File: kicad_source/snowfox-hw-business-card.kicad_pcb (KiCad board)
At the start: 2 copper layers, 39 x 46 mm, 14 parts, among them CN1 TE_2041119-2, CN2 CONN_01X18, CN3 CONN_01X18

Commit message: started placement
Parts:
- removed G***: generationmake_logo, labels:generationmake_logo
- removed G***: generationmake_small_solder, labels:generationmake_small_solder
- removed MECH4, MECH5: MHP_3.2_5.8, MECH_mounting_holes:MHP_3.2_5.8
- removed W1, W2: TEST_1P, wire_pads:SolderWirePad_single_1mmSMD
- added BT1: Keystone 1043, MECH_battery_holder:KEYSTONE_1043, F.Cu at (81.0, 47.0)
- added BT2: Keystone 1043, MECH_battery_holder:KEYSTONE_1043, F.Cu at (187.0, 51.0)
- added C1: 100n, capacitors:C_0603, F.Cu at (253.3, 84.3)
- added C10: 100n, capacitors:C_0603, F.Cu at (253.3, 86.9)
- added C11: 100n, capacitors:C_0603, F.Cu at (250.0, 90.0)
- added C12: 100n, capacitors:C_0603, F.Cu at (257.2, 82.9)
- added C13: 100n, capacitors:C_0603, F.Cu at (245.8, 97.6)
- added C14: 100n, capacitors:C_0603, F.Cu at (264.5, 80.3)
- added C15: 100n, capacitors:C_0603, F.Cu at (257.2, 85.4)
- added C16: 100n, capacitors:C_0603, F.Cu at (249.7, 92.5)
- added C17: 100n, capacitors:C_0603, F.Cu at (264.5, 77.8)
- added C18: 1u 50V, capacitors:C_0603, F.Cu at (240.8, 109.5)
- added C19: 1u 50V, capacitors:C_0603, F.Cu at (240.6, 104.4)
- added C2: 100n, capacitors:C_0603, F.Cu at (256.6, 77.8)
- added C20: 1u 50V, capacitors:C_0603, F.Cu at (236.5, 113.7)
- added C21: 1u 50V, capacitors:C_0603, F.Cu at (244.8, 107.0)
- added C22: 1u 50V, capacitors:C_0603, F.Cu at (240.8, 107.0)
- added C23: 1u 50V, capacitors:C_0603, F.Cu at (244.5, 104.4)
- added C24: 1u 50V, capacitors:C_0603, F.Cu at (236.9, 110.1)
- added C25: 1u 50V, capacitors:C_0603, F.Cu at (227.0, 115.8)
- added C26: 1u 50V, capacitors:C_0603, F.Cu at (232.5, 113.7)
- added C27: 470n 50V, capacitors:C_0603, F.Cu at (236.9, 107.6)
- added C28: 10u, capacitors:C_0603, F.Cu at (183.8, 127.1)
- added C29: 100n, capacitors:C_0603, F.Cu at (183.4, 131.3)
- added C3: 15p, capacitors:C_0603, F.Cu at (256.6, 80.3)
- added C30: 10u, capacitors:C_0603, F.Cu at (197.6, 119.7)
- added C31: 100n, capacitors:C_0603, F.Cu at (179.5, 131.3)
- added C32: 1u, capacitors:C_0603, F.Cu at (189.7, 113.2)
- added C33: 1u, capacitors:C_0603, F.Cu at (219.6, 112.6)
- added C34: 1u, capacitors:C_0603, F.Cu at (215.7, 112.6)
- added C35: 1u, capacitors:C_0603, F.Cu at (219.6, 110.1)
- added C36: 1u, capacitors:C_0603, F.Cu at (215.7, 110.1)
- added C37: 100u/6.3V, capacitors:TantalC_SizeD_EIA-7343_Reflow, F.Cu at (182.6, 111.9)
- added C38: 100u/6.3V, capacitors:TantalC_SizeD_EIA-7343_Reflow, F.Cu at (214.8, 79.6)
- added C39: DNI, capacitors:C_0603, F.Cu at (121.0, 120.0)
- added C4: 15p, capacitors:C_0603, F.Cu at (246.1, 90.0)
- added C40: 100nF, capacitors:C_0603, F.Cu at (117.0, 115.0)
- added C5: 10u, capacitors:C_0603, F.Cu at (260.6, 77.8)
- added C6: 10u, capacitors:C_0603, F.Cu at (245.8, 92.5)
- added C7: 100n, capacitors:C_0603, F.Cu at (260.6, 80.3)
- added C8: 100n, capacitors:C_0603, F.Cu at (249.7, 95.1)
- added C9: 100n, capacitors:C_0603, F.Cu at (245.8, 95.1)
- added D2: MBR0530, diodes:SOD-123, F.Cu at (235.8, 104.7)
- added D3: MBR0530, diodes:SOD-123, F.Cu at (227.8, 109.8)
- added D4: MBR0530, diodes:SOD-123, F.Cu at (227.8, 112.9)
- added D5: green, LEDs:LED_0603, F.Cu at (187.3, 131.3)
- added D6: red, LEDs:LED_0603, F.Cu at (201.5, 119.7)
- added D7: MBR0530, diodes:SOD-123, F.Cu at (190.5, 110.4)
- added D8: 1N4148, diodes:SOD-123, F.Cu at (201.6, 110.4)
- added D9: 1N4148, diodes:SOD-123, F.Cu at (196.1, 110.4)
- added L1: INDUCTOR_SMALL, inductors:Inductor_1212, F.Cu at (229.0, 105.7)
- added P1: USB_OTG, CON_wuerth:WE_629105136821, F.Cu at (158.0, 104.0)
- added Q1: SI1304BDL, SOT_TO:SOT-23, F.Cu at (232.7, 110.3)
- added Q2: BC847, SOT_TO:SOT-23, F.Cu at (179.7, 127.9)
- added Q3: BC847, SOT_TO:SOT-23, F.Cu at (190.5, 127.9)
- added R10: 10k, resistors:R_0603, F.Cu at (257.5, 88.0)
- added R11: 10k, resistors:R_0603, F.Cu at (249.6, 97.7)
- added R12: 10k, resistors:R_0603, F.Cu at (253.8, 92.1)
- added R13: 10k, resistors:R_0603, F.Cu at (253.8, 89.5)
- added R14: 10k, resistors:R_0603, F.Cu at (261.0, 82.9)
- added R15: 2R2, resistors:R_0603, F.Cu at (240.3, 115.4)
- added R16: DNI, resistors:R_0603, F.Cu at (244.6, 109.6)
- added R17: 0R, resistors:R_0603, F.Cu at (240.3, 112.7)
- added R18: 22k1, resistors:R_0603, F.Cu at (201.8, 124.9)
- added R19: 47k5, resistors:R_0603, F.Cu at (198.4, 127.6)
- added R2: 100k, resistors:R_0603, F.Cu at (264.8, 85.6)
- added R20: 1k, resistors:R_0603, F.Cu at (198.4, 130.2)
- added R21: 1k, resistors:R_0603, F.Cu at (194.5, 127.1)
- added R22: 100R, resistors:R_0603, F.Cu at (194.7, 129.7)
- added R23: 100R, resistors:R_0603, F.Cu at (198.1, 124.9)
- added R24: 1k, resistors:R_0603, F.Cu at (201.1, 122.3)
- added R25: 10k, resistors:R_0603, F.Cu at (191.1, 131.3)
- added R26: 10k, resistors:R_0603, F.Cu at (197.5, 122.3)
- added R27: 150k, resistors:R_0603, F.Cu at (193.5, 113.3)
- added R28: 10k, resistors:R_0603, F.Cu at (120.0, 110.0)
- added R3: 1M, resistors:R_0603, F.Cu at (253.2, 97.7)
- added R4: 100R, resistors:R_0603, F.Cu at (261.1, 88.2)
- added R5: 100R, resistors:R_0603, F.Cu at (257.5, 93.3)
- added R6: 100R, resistors:R_0603, F.Cu at (261.1, 85.6)
- added R7: 100R, resistors:R_0603, F.Cu at (264.7, 82.9)
- added R8: 100, resistors:R_0603, F.Cu at (253.5, 94.8)
- added R9: 10k, resistors:R_0603, F.Cu at (257.5, 90.7)
- added SW1: TAST_VER, mechanical-switches:WE_430182050816, F.Cu at (144.0, 133.0)
- added SW2: TAST_VER, mechanical-switches:WE_430182050816, F.Cu at (84.0, 133.0)
- added SW3: TAST_VER, mechanical-switches:WE_430182050816, F.Cu at (101.0, 133.0)
- added SW4: TAST_VER, mechanical-switches:WE_430182050816, F.Cu at (156.0, 133.0)
- added SW5: SWITCH_INV, mechanical-switches:WE_450404015514, F.Cu at (150.0, 85.0)
- added U1: W25Q80D, SOIC:SOIC-8_3.9x4.9mm_Pitch1.27mm, F.Cu at (96.0, 98.0)
- added U2: ATECC608A, SOIC:SOIC-8_3.9x4.9mm_Pitch1.27mm, F.Cu at (239.8, 87.1)
- added U3: FE310-G002, QFN:QFN-48-1EP_6x6mm_P0.4mm_EP4.3x4.3mm, F.Cu at (105.0, 103.0)
- added U4: CP2102N_28, QFN:QFN-28-1EP_5x5mm_Pitch0.5mm, F.Cu at (148.8, 104.2)
- added U5: TPS736XX, SOT_TO:SOT-23-5, F.Cu at (211.4, 111.2)
- added U6: TPS736XX, SOT_TO:SOT-23-5, F.Cu at (206.7, 111.2)
- added U7: M24LR, SOIC:SOIC-8_3.9x4.9mm_Pitch1.27mm, F.Cu at (121.0, 115.0)
- added Y1: Crystal_SMD_4Pad, crystals:Crystal_SMD_0603_4Pads, F.Cu at (247.7, 86.3)
- CN1: value TE_2041119-2 -> Micro_SDCard; footprint connectors_pci-express:MPCIe_4mm -> CON_wuerth:WE_693071010811
- CN2: value CONN_01X18 -> CONN_02X05; footprint pin_headers:Pin_Header_Straight_1x18 -> pin_headers:Pin_Header_Straight_2x05_Pitch1.27mm
- CN3: value CONN_01X18 -> CONN_01X24; footprint pin_headers:Pin_Header_Straight_1x18 -> pin_headers:Pin_Header_Angled_1x24_Pitch1.00mm
- D1: value 150060YS75000 -> blue
- MECH1, MECH2: value WA-SMSI_9774015151 -> MHP_3.2_5.8; footprint MECH_smd-spacer:WA-SMSI_9774015151 -> MECH_mounting_holes:MHP_3.2_5.8
- R1: value 3k3 -> 1k
- moved MECH3 151.8 mm to (238.3, 64.9)
- moved MECH2 132.1 mm to (231.5, 64.9)
- moved R1 118.7 mm to (194.4, 92.2), turned to 0 degrees
- moved D1 110.8 mm to (189.0, 100.6), turned to 0 degrees
- moved MECH1 77.4 mm to (159.0, 87.0)
- moved CN3 60.5 mm to (80.0, 97.0), turned to 0 degrees
- moved CN2 42.8 mm to (102.0, 113.0), turned to 90 degrees
- moved CN1 42.4 mm to (124.0, 99.0), turned to 180 degrees
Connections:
- CN1 pad 1: /PEX_PIN1 -> (no net)
- CN1 pad 10: /PEX_PIN10 -> (no net)
- CN1 pad 2: +3V3 -> /Microcontroller/SPI_CS_SD_R
- CN1 pad 3: /PEX_PIN3 -> /Microcontroller/SPI_MOSI_R
- CN1 pad 4: GND -> +3V3
- CN1 pad 5: /PEX_PIN5 -> /Microcontroller/SPI_CLK_R
- CN1 pad 6: /PEX_PIN6 -> GND
- CN1 pad 7: /PEX_PIN7 -> /Microcontroller/SPI_MISO_R
- CN1 pad 8: /PEX_PIN8 -> (no net)
- CN1 pad 9: GND -> (no net)
- CN2 pad 1: +3V3 -> (no net)
- CN2 pad 10: /PEX_PIN12 -> RESET
- CN2 pad 2: /PEX_PIN1 -> /Microcontroller/JTAG_TMS
- CN2 pad 3: /PEX_PIN3 -> GND
- CN2 pad 4: /PEX_PIN5 -> /Microcontroller/JTAG_TCK
- CN2 pad 5: /PEX_PIN6 -> GND
- CN2 pad 6: /PEX_PIN7 -> /Microcontroller/JTAG_TDO
- CN2 pad 7: /PEX_PIN8 -> (no net)
- CN2 pad 8: /PEX_PIN10 -> /Microcontroller/JTAG_TDI
- CN2 pad 9: /PEX_PIN11 -> (no net)
- CN3 pad 1: +3V3 -> (no net)
- CN3 pad 10: /PEX_PIN33 -> DIS_RESET#
- CN3 pad 11: /PEX_PIN32 -> DIS_D_C#
- CN3 pad 12: /PEX_PIN31 -> SPI_CS_DIS
- CN3 pad 13: /PEX_PIN30 -> SPI_CLK
- CN3 pad 14: /PEX_PIN28 -> SPI_MOSI
- CN3 pad 15: /PEX_PIN25 -> +3V3
- CN3 pad 16: /PEX_PIN23 -> +3V3
- CN3 pad 18: GND -> /Display/VDD
- CN3 pad 2: /PEX_PIN51 -> /Display/GDR
- CN3 pad 3: /PEX_PIN49 -> /Display/RESE
- CN3 pad 4: /PEX_PIN48 -> (no net)
- CN3 pad 5: /PEX_PIN47 -> /Display/VSH2
- CN3 pad 6: /PEX_PIN46 -> (no net)
- CN3 pad 7: /PEX_PIN45 -> (no net)
- CN3 pad 8: /PEX_PIN44 -> /Display/BSI
- CN3 pad 9: /PEX_PIN42 -> DIS_BUSY
- R1 pad 2: +3V3 -> /Microcontroller/LED
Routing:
- net +3V3: track 101.7 -> 0.00 mm, vias 6 -> 0
- net /NFC/ANTENNA: track 0.00 -> 93.2 mm
- net GND: track 66.1 -> 0.00 mm, vias 15 -> 0
- net /PEX_PIN23: track 35.2 -> 0.00 mm, vias 1 -> 0
- net /PEX_RST: track 32.0 -> 0.00 mm
- net /PEX_PIN25: track 31.8 -> 0.00 mm, vias 1 -> 0
- net /WM_PIO25: track 30.5 -> 0.00 mm
- net /WM_PIO24: track 29.0 -> 0.00 mm
- net /PEX_PIN20: track 26.3 -> 0.00 mm
- net /PEX_PIN48: track 23.5 -> 0.00 mm, vias 1 -> 0
- net /PEX_PIN28: track 23.1 -> 0.00 mm
- net /PEX_PIN31: track 22.8 -> 0.00 mm, vias 1 -> 0
- net /PEX_PIN46: track 19.9 -> 0.00 mm, vias 1 -> 0
- net /PEX_PIN30: track 19.8 -> 0.00 mm
- net /PEX_PIN13: track 18.1 -> 0.00 mm
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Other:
- board size 39 x 46 mm -> 85 x 54 mm
- board text removed: "3V3"
- board text removed: "GND"
- board text removed: "Licensed under CERN OHL v.1.2"
- board text removed: "P1"
- board text removed: "P10"
- board text removed: "P10 (3)"
- board text removed: "P11"
- board text removed: "P11(19)"
- board text removed: "P12"
- board text removed: "P12(4)"
- board text removed: "P13"
- board text removed: "P13(20)"
- board text removed: "P14"
- board text removed: "P14(5)"
- board text removed: "P16"
- board text removed: "P16(6)"
- board text removed: "P20"
- board text removed: "P20(7)"
- board text removed: "P23"
- board text removed: "P23(21)"
- board text removed: "P25"
- board text removed: "P25(22)"
- board text removed: "P28"
- board text removed: "P28(8)"
- board text removed: "P3"
- board text removed: "P30"
- board text removed: "P30(9)pu"
- board text removed: "P31"
- board text removed: "P31(23)"
- board text removed: "P32"
- board text removed: "P32(10)pu"
- board text removed: "P33"
- board text removed: "P33(24)"
- board text removed: "P42"
- board text removed: "P42(11)"
- board text removed: "P44"
- board text removed: "P44(12)"
- board text removed: "P45"
- board text removed: "P45(13)"
- board text removed: "P46"
- board text removed: "P46(14)"
- board text removed: "P47"
- board text removed: "P47(15)"
- board text removed: "P48"
- board text removed: "P48(16)"
- board text removed: "P49"
- board text removed: "P49 (17)"
- board text removed: "P5"
- board text removed: "P51"
- board text removed: "P51 (18)"
- board text removed: "P6"
- board text removed: "P6(1)"
- board text removed: "P7"
- board text removed: "P8"
- board text removed: "P8(2)"
- board text removed: "PWR"
- board text removed: "RST"
- board text removed: "RST (0)pu"
- board text removed: "VidorBreakout 1.0"
- board text removed: "WM_PIO24"
- board text removed: "WM_PIO25"
- board text removed: "bot"
- board text removed: "top"
- board text removed: "use with Arduino MKR Vidor 4000"
- board text removed: "visit www.generationmake.de for more information!"

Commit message: made first placement
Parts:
- BT1, BT2: value Keystone 1043 -> 79523141; footprint MECH_battery_holder:KEYSTONE_1043 -> MECH_battery_holder:Wuerth_WA-BCMC_79523141
- moved R2 177.9 mm to (88.0, 106.0), turned to 90 degrees
- moved C15 171.9 mm to (92.0, 133.0)
- moved R7 171.5 mm to (97.0, 119.0)
- moved R4 168.2 mm to (97.0, 125.0)
- moved C3 168.0 mm to (92.0, 114.0), turned to 180 degrees
- moved R6 167.9 mm to (97.0, 121.0)
- moved R12 166.4 mm to (92.0, 131.0)
- moved C1 164.7 mm to (90.0, 106.0), turned to 270 degrees
- moved C5 164.2 mm to (99.0, 107.0), turned to 180 degrees
- moved C16 163.3 mm to (92.0, 135.0)
- moved R5 163.2 mm to (97.0, 123.0)
- moved R16 162.3 mm to (83.0, 95.0), turned to 270 degrees
- moved C21 160.8 mm to (84.0, 110.0), turned to 180 degrees
- moved C23 160.6 mm to (84.0, 108.0)
- moved MECH3 158.3 mm to (81.5, 86.5)
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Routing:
- net /NFC/ANTENNA: track 93.2 -> 250.4 mm, vias 0 -> 2

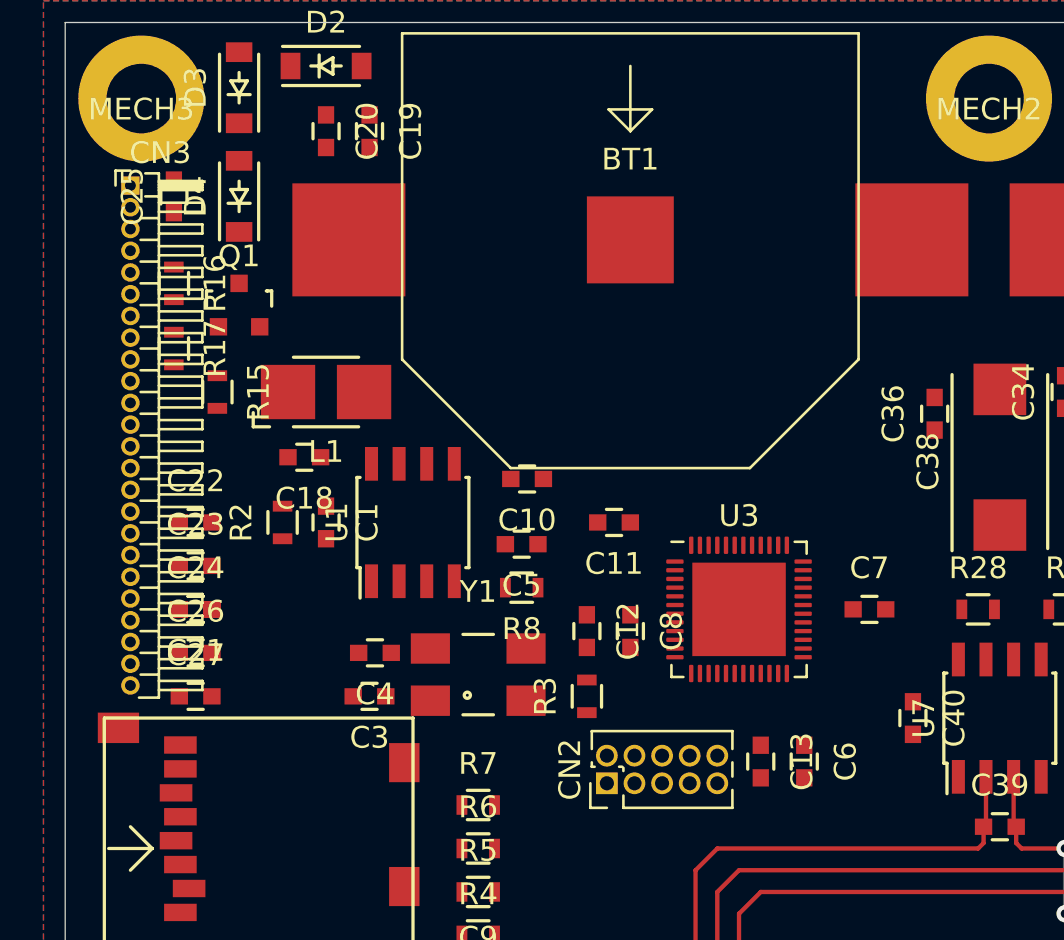
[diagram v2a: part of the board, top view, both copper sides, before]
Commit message: changed connector for display
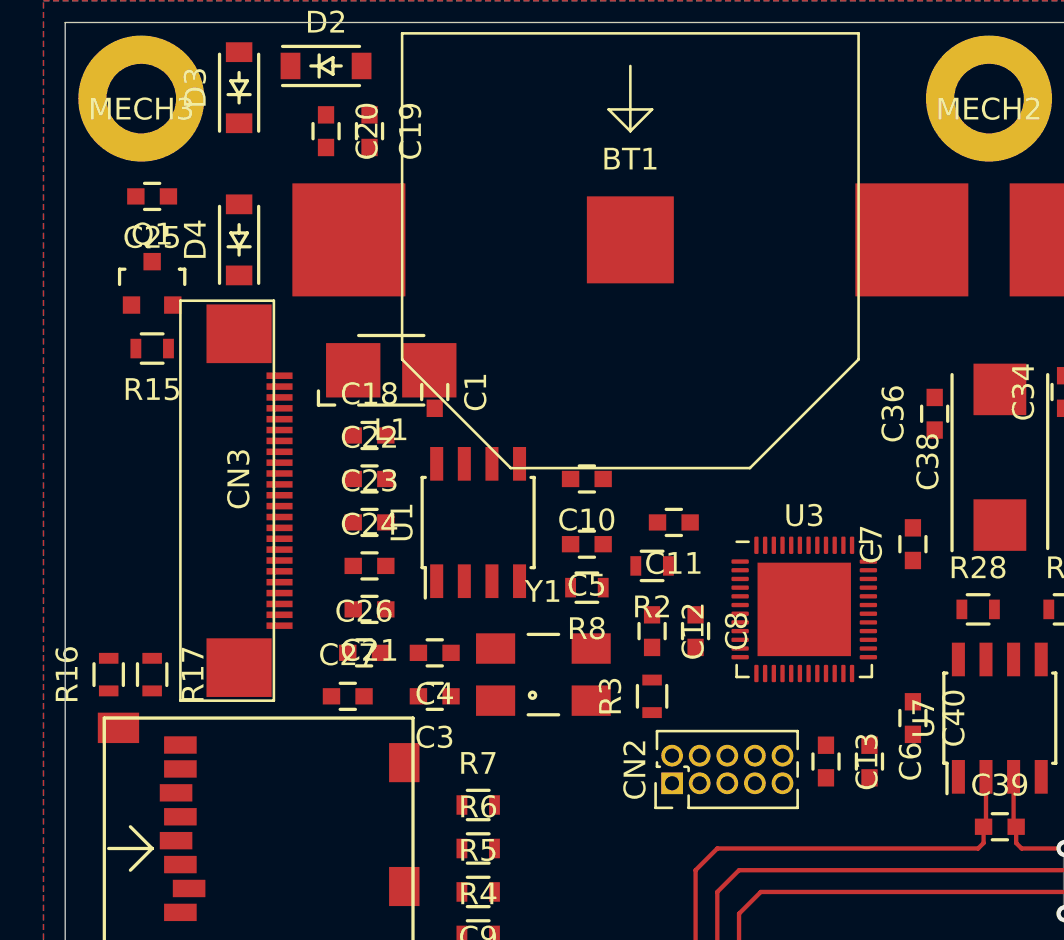
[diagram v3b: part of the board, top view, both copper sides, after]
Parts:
- CN3: footprint pin_headers:Pin_Header_Angled_1x24_Pitch1.00mm -> CON_wuerth:WR-FPC_68712414522
- Y1: value Crystal_SMD_4Pad -> 16MHz
- moved R16 18.2 mm to (80.0, 113.0), turned to 90 degrees
- moved R2 17.1 mm to (105.0, 108.0), turned to 180 degrees
- moved CN3 15.3 mm to (86.0, 105.0), turned to 270 degrees
- moved R17 15.0 mm to (82.0, 113.0)
- moved C22 8.25 mm to (92.0, 104.0)
- moved C23 8.25 mm to (92.0, 106.0)
- moved C24 8.25 mm to (92.0, 108.0)
- moved C21 8.00 mm to (92.0, 110.0)
- moved C1 7.81 mm to (95.0, 100.0)
- moved C26 7.75 mm to (91.8, 112.0)
- moved C27 7.00 mm to (91.0, 114.0)
- moved Q1 4.12 mm to (82.0, 95.0)
- moved C7 3.61 mm to (117.0, 107.0), turned to 90 degrees
- moved R15 3.61 mm to (82.0, 98.0), turned to 180 degrees
- moved C18 3.16 mm to (92.0, 102.0), turned to 0 degrees
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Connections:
- CN2 pad 1: (no net) -> +3V3

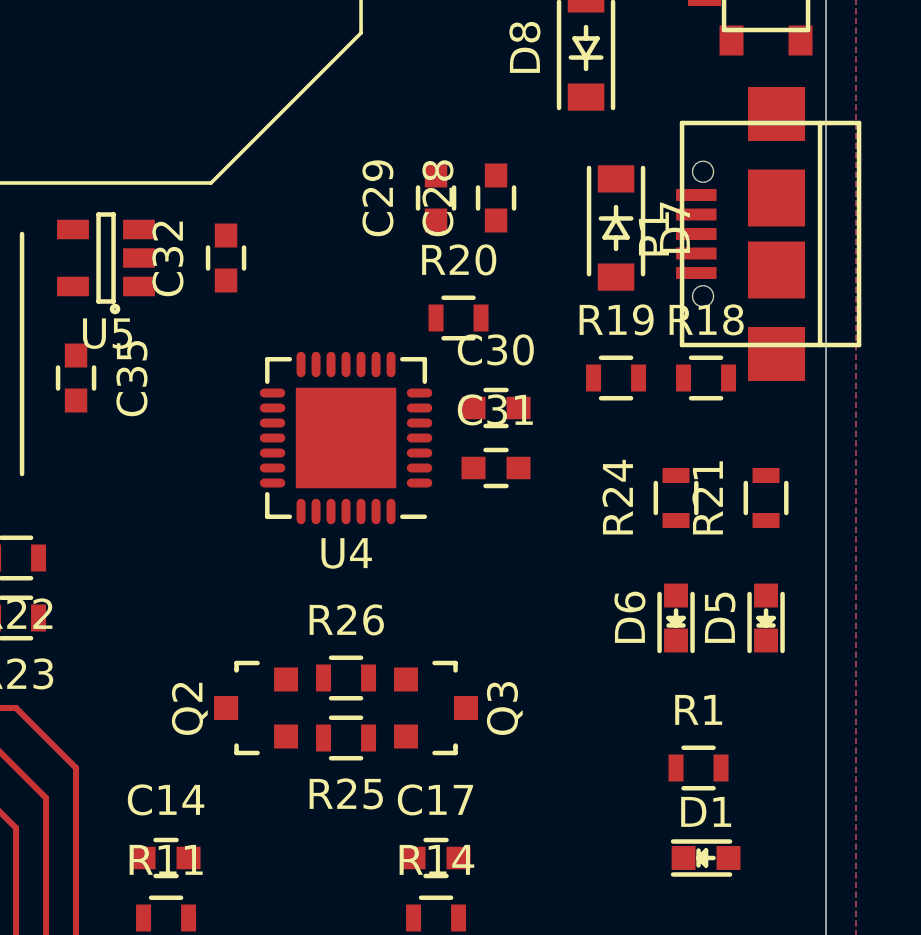
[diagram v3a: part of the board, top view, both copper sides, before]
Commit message: changed usb controller to FTDI FT230XS
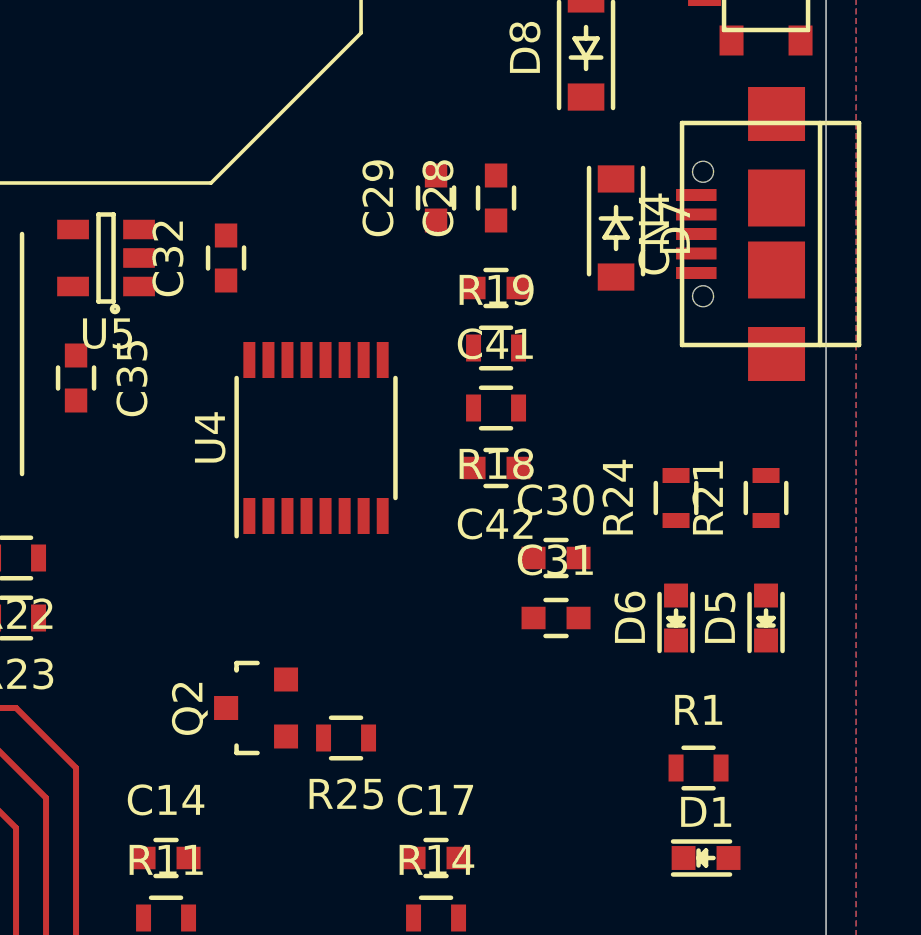
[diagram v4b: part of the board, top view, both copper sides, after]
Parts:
- removed Q3: BC847, SOT_TO:SOT-23
- removed R20: 1k, resistors:R_0603
- removed R26: 10k, resistors:R_0603
- added C41: 47pF, capacitors:C_0603, F.Cu at (152.0, 107.0)
- added C42: 47pF, capacitors:C_0603, F.Cu at (152.0, 113.0)
- R18: value 22k1 -> 27R
- R19: value 47k5 -> 27R
- U4: value CP2102N_28 -> FT230XS; footprint QFN:QFN-28-1EP_5x5mm_Pitch0.5mm -> SSOP:SSOP-16_3.9x4.9mm_Pitch0.635mm
- moved R18 7.07 mm to (152.0, 111.0), turned to 180 degrees
- moved C30 5.39 mm to (154.0, 116.0)
- moved C31 5.39 mm to (154.0, 118.0)
- moved R19 4.12 mm to (152.0, 109.0)
- moved U4 1.00 mm to (146.0, 112.0), turned to 90 degrees
- renumbered P1 to CN4
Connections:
- CN4 pad 2: Net-(P1-Pad2) -> /USB/USBDM
- CN4 pad 3: Net-(P1-Pad3) -> /USB/USBDP
- D5 pad 1: Net-(D5-Pad1) -> /USB/RX_LED
- D6 pad 1: Net-(D6-Pad1) -> /USB/TX_LED
- Q2 pad 1: /USB/DTR_R -> /USB/RTS_R
- Q2 pad 2: /USB/RTS -> GND
- R18 pad 1: Net-(R18-Pad1) -> /USB/USBDM
- R18 pad 2: VIN -> /USB/USBDM_R
- R19 pad 1: GND -> /USB/USBDP_R
- R19 pad 2: Net-(R18-Pad1) -> /USB/USBDP
- R25 pad 1: /USB/DTR -> /USB/RTS
- R25 pad 2: /USB/DTR_R -> /USB/RTS_R
- U4 pad 1: (no net) -> /USB/TX_R
- U4 pad 10: (no net) -> VIO
- U4 pad 11: (no net) -> VIO
- U4 pad 12: (no net) -> VIN
- U4 pad 13: (no net) -> GND
- U4 pad 14: (no net) -> /USB/RX_LED
- U4 pad 2: (no net) -> /USB/RTS
- U4 pad 3: GND -> VIO
- U4 pad 4: Net-(P1-Pad3) -> /USB/RX_R
- U4 pad 5: Net-(P1-Pad2) -> GND
- U4 pad 6: VIO -> (no net)
- U4 pad 7: VIN -> /USB/TX_LED
- U4 pad 8: Net-(R18-Pad1) -> /USB/USBDP_R
- U4 pad 9: Net-(R20-Pad1) -> /USB/USBDM_R

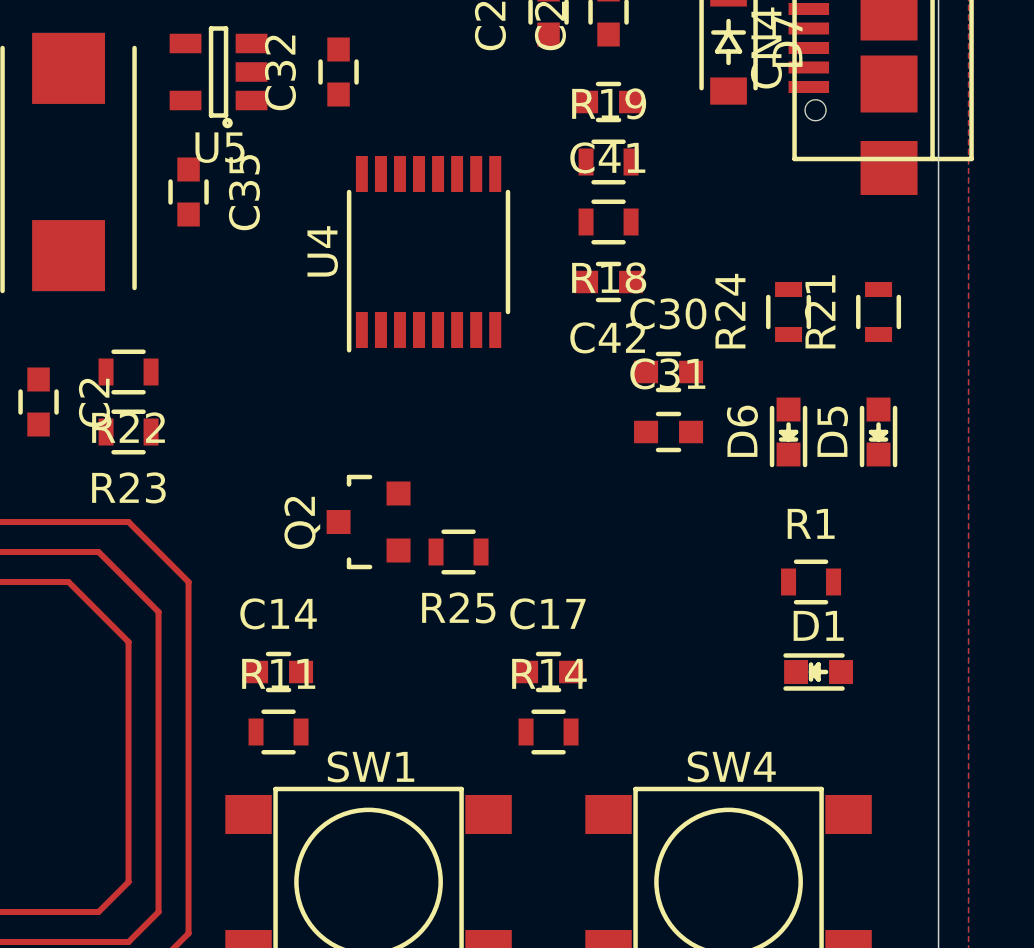
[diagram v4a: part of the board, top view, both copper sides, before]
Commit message: added qwiic connector for I2C and grove connector for UART
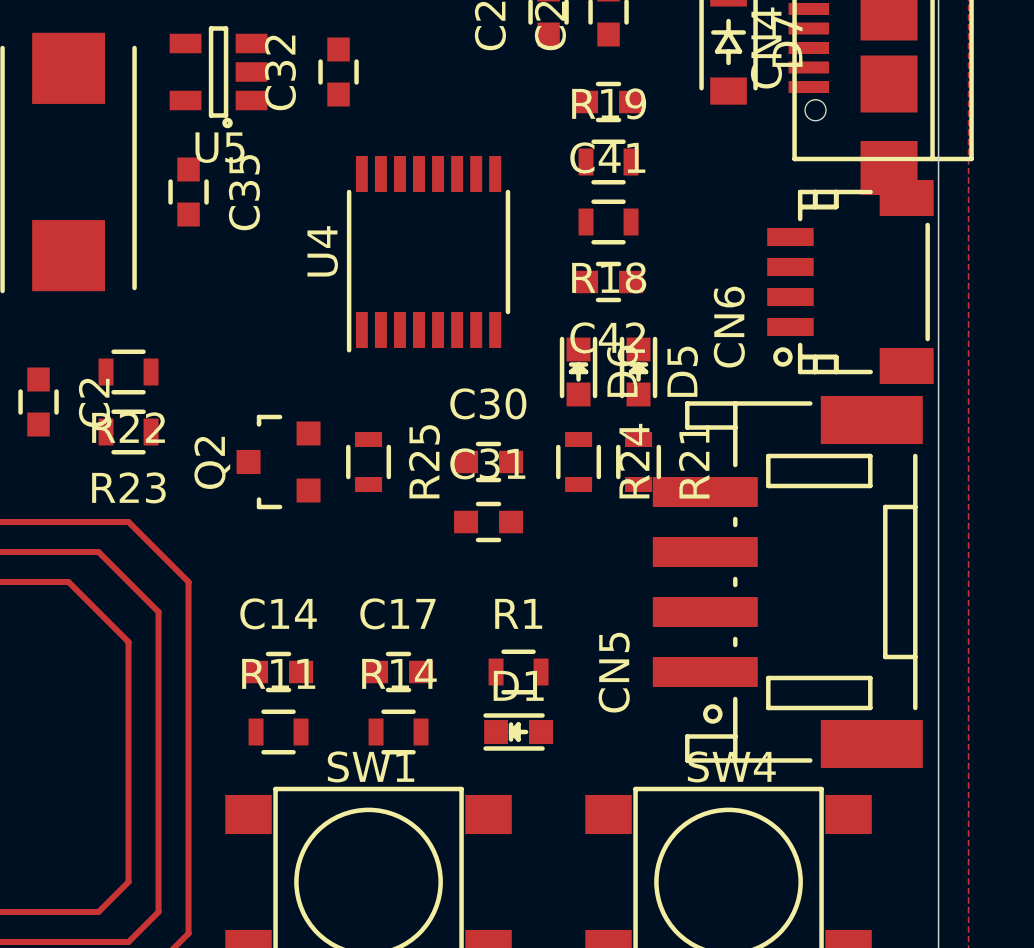
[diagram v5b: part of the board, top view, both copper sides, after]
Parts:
- added CN5: CONN_01X04, connectors_JST_PH:Connectors_JST_S4B-PH-SM4-TB, F.Cu at (158.0, 123.0)
- added CN6: CONN_01X04, connectors_JST_SH:Connectors_JST_SM04B-SRSS-TB, F.Cu at (160.0, 113.0)
- moved R1 10.2 mm to (149.0, 126.0)
- moved D1 10.2 mm to (149.0, 128.0)
- moved R21 9.43 mm to (153.0, 119.0), turned to 270 degrees
- moved R24 8.60 mm to (151.0, 119.0), turned to 270 degrees
- moved D5 8.25 mm to (153.0, 116.0), turned to 270 degrees
- moved D6 7.28 mm to (151.0, 116.0), turned to 270 degrees
- moved C30 6.71 mm to (148.0, 119.0)
- moved C31 6.71 mm to (148.0, 121.0)
- moved C17 5.00 mm to (145.0, 126.0)
- moved R14 5.00 mm to (145.0, 128.0)
- moved R25 4.24 mm to (144.0, 119.0), turned to 270 degrees
- moved Q2 3.61 mm to (141.0, 119.0)
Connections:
- U3 pad 40: (no net) -> /Microcontroller/EXT_TX
- U3 pad 45: (no net) -> /Microcontroller/EXT_RX
